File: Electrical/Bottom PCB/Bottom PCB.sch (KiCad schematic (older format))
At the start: 39 parts, among them J1 Steper1, J10 Servo4, J2 Steper2, J3 H Bridge, J4 4 x OP, J6 Servo1, J7 Servo2, J8 Servo3, J9 MainIO, SW1 FL, SW2 FR, U1 ULN2003A, U2 74HC595, U3 QRE1113, U4 TB6612FNG, U5 74HC595, U6 QRE1113, U7 QRE1113, U8 QRE1113

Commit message: small update
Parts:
- added C1, C11, C14, C2, C4, C7, C9: 100pF, Capacitor_SMD:C_1206_3216Metric_Pad1.42x1.75mm_HandSolder, symbol Device:C_Small
- added C10, C12, C3, C6, C8: 10uF, Capacitor_SMD:C_1206_3216Metric_Pad1.42x1.75mm_HandSolder, symbol Device:C_Small
- C13: renamed from C2; value 10pF -> 100pF; footprint Capacitor_SMD:C_1210_3225Metric_Pad1.42x2.65mm_HandSolder -> Capacitor_SMD:C_1206_3216Metric_Pad1.42x1.75mm_HandSolder
- C15: renamed from C3; value 10pF -> 100pF; footprint Capacitor_SMD:C_1210_3225Metric_Pad1.42x2.65mm_HandSolder -> Capacitor_SMD:C_1206_3216Metric_Pad1.42x1.75mm_HandSolder
- C16: renamed from C4; value 10pF -> 100pF
- C17: renamed from C5; value 10pF -> 100pF; footprint Capacitor_SMD:C_1210_3225Metric_Pad1.42x2.65mm_HandSolder -> Capacitor_SMD:C_1206_3216Metric_Pad1.42x1.75mm_HandSolder
- C5: renamed from C1; value 10pF -> 100pF; footprint Capacitor_SMD:C_1210_3225Metric_Pad1.42x2.65mm_HandSolder -> Capacitor_SMD:C_1206_3216Metric_Pad1.42x1.75mm_HandSolder
- J8: renamed from J9; footprint Connector_JST:JST_XH_B5B-XH-A_1x06_P2.50mm_Vertical -> Connector_PinHeader_2.54mm:PinHeader_1x06_P2.54mm_Vertical
- R1, R10, R11, R12, R2, R3, R4, R5, R6, R7, R8, R9: footprint Resistor_SMD:R_1210_3225Metric_Pad1.42x2.65mm_HandSolder -> Resistor_SMD:R_1206_3216Metric_Pad1.42x1.75mm_HandSolder
- renumbered J6 to J5, J7 to J6, J8 to J7, J10 to J9
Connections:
- wire segments 269 -> 294

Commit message: PCB
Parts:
- C16: footprint Capacitor_SMD:C_1210_3225Metric_Pad1.42x2.65mm_HandSolder -> Capacitor_SMD:C_1206_3216Metric_Pad1.42x1.75mm_HandSolder
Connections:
- wire segments 294 -> 295
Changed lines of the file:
@@
 Text GLabel 9350 3350 0    50   Input ~ 0
 Servo1
-Text GLabel 9350 3850 0    50   Input ~ 0
-Servo3
 Text GLabel 9350 3950 0    50   Input ~ 0
 Servo4
@@
 Wire Wire Line
 	6800 3800 6650 3800
-Text GLabel 9350 3650 0    50   Input ~ 0
-M1PWM
-Text GLabel 9350 3750 0    50   Input ~ 0
-M2PWM
 Text GLabel 5300 3300 0    50   Input ~ 0
 M2PWM
@@
 F 0 "C16" H 1492 5696 50  0000 L CNN
 F 1 "100pF" H 1492 5605 50  0000 L CNN
-F 2 "Capacitor_SMD:C_1210_3225Metric_Pad1.42x2.65mm_HandSolder" H 1400 5650 50  0001 C CNN
+F 2 "Capacitor_SMD:C_1206_3216Metric_Pad1.42x1.75mm_HandSolder" H 1400 5650 50  0001 C CNN
 F 3 "~" H 1400 5650 50  0001 C CNN
 	1    1400 5650
@@
 	11100 800  11250 800
 Connection ~ 11100 800
+Wire Wire Line
+	10500 3950 10650 3950
+Text GLabel 9350 3850 0    50   Input ~ 0
+Servo3
+Text GLabel 9350 3750 0    50   Input ~ 0
+M2PWM
+Text GLabel 9350 3650 0    50   Input ~ 0
+M1PWM
 $EndSCHEMATC

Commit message: Changed IR sensors to allow for passive measurments
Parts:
- removed J4: 4 x OP, Connector_PinHeader_2.54mm:PinHeader_1x04_P2.54mm_Vertical, symbol Connector_Generic:Conn_01x04
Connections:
- net labels added: IR

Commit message: Adding 9 DoF IMU
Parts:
- added C?: 10uF, Capacitor_SMD:C_1206_3216Metric_Pad1.42x1.75mm_HandSolder, symbol Device:C_Small
- added C?: 100pF, Capacitor_SMD:C_1206_3216Metric_Pad1.42x1.75mm_HandSolder, symbol Device:C_Small
- added U9: MPU-9250, Sensor_Motion:InvenSense_QFN-24_3x3mm_P0.4mm, symbol Sensor_Motion:MPU-9250
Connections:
- net labels added: +3.3V
- wire segments 295 -> 298
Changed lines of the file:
@@
 Text GLabel 550  6450 1    50   Input ~ 0
 IR
+$Comp
+L Sensor_Motion:MPU-9250 U9
+U 1 1 5ECB7562
+P 4500 6250
+F 0 "U9" H 4500 5261 50  0000 C CNN
+F 1 "MPU-9250" H 4500 5170 50  0000 C CNN
+F 2 "Sensor_Motion:InvenSense_QFN-24_3x3mm_P0.4mm" H 4500 5250 50  0001 C CNN
+F 3 "https://store.invensense.com/datasheets/invensense/MPU9250REV1.0.pdf" H 4500 6100 50  0001 C CNN
+	1    4500 6250
+	1    0    0    -1
+$EndComp
+$Comp
+L power:GND #PWR?
+U 1 1 5ECC16E7
+P 4500 7150
+F 0 "#PWR?" H 4500 6900 50  0001 C CNN
+F 1 "GND" H 4505 6977 50  0000 C CNN
+F 2 "" H 4500 7150 50  0001 C CNN
+F 3 "" H 4500 7150 50  0001 C CNN
+	1    4500 7150
+	1    0    0    -1
+$EndComp
+$Comp
+L power:GND #PWR?
+U 1 1 5ECC2609
+P 5350 7150
+F 0 "#PWR?" H 5350 6900 50  0001 C CNN
+F 1 "GND" H 5355 6977 50  0000 C CNN
+F 2 "" H 5350 7150 50  0001 C CNN
+F 3 "" H 5350 7150 50  0001 C CNN
+	1    5350 7150
+	1    0    0    -1
+$EndComp
+Wire Wire Line
+	5200 6650 5350 6650
+Wire Wire Line
+	5350 6650 5350 7150
+$Comp
+L power:+3.3V #PWR?
+U 1 1 5ECDED5D
+P 4600 5250
+F 0 "#PWR?" H 4600 5100 50  0001 C CNN
+F 1 "+3.3V" H 4615 5423 50  0000 C CNN
+F 2 "" H 4600 5250 50  0001 C CNN
+F 3 "" H 4600 5250 50  0001 C CNN
+	1    4600 5250
+	1    0    0    -1
+$EndComp
+Wire Wire Line
+	4600 5250 4600 5350
+$Comp
+L power:+3.3V #PWR?
+U 1 1 5ECFA0AC
+P 5450 5250
+F 0 "#PWR?" H 5450 5100 50  0001 C CNN
+F 1 "+3.3V" H 5465 5423 50  0000 C CNN
+F 2 "" H 5450 5250 50  0001 C CNN
+F 3 "" H 5450 5250 50  0001 C CNN
+	1    5450 5250
+	1    0    0    -1
+$EndComp
+$Comp
+L Device:C_Small C?
+U 1 1 5ECFABED
+P 5450 5350
+F 0 "C?" H 5542 5396 50  0000 L CNN
+F 1 "10uF" H 5542 5305 50  0000 L CNN
+F 2 "Capacitor_SMD:C_1206_3216Metric_Pad1.42x1.75mm_HandSolder" H 5450 5350 50  0001 C CNN
+F 3 "~" H 5450 5350 50  0001 C CNN
+	1    5450 5350
+	1    0    0    -1
+$EndComp
+$Comp
+L Device:C_Small C?
+U 1 1 5ECFB59E
+P 5800 5350
+F 0 "C?" H 5892 5396 50  0000 L CNN
+F 1 "100pF" H 5892 5305 50  0000 L CNN
+F 2 "Capacitor_SMD:C_1206_3216Metric_Pad1.42x1.75mm_HandSolder" H 5800 5350 50  0001 C CNN
+F 3 "~" H 5800 5350 50  0001 C CNN
+	1    5800 5350
+	1    0    0    -1
+$EndComp
+$Comp
+L power:+3.3V #PWR?
+U 1 1 5ECFBDFF
+P 5800 5250
+F 0 "#PWR?" H 5800 5100 50  0001 C CNN
+F 1 "+3.3V" H 5815 5423 50  0000 C CNN
+F 2 "" H 5800 5250 50  0001 C CNN
+F 3 "" H 5800 5250 50  0001 C CNN
+	1    5800 5250
+	1    0    0    -1
+$EndComp
+$Comp
+L power:GND #PWR?
+U 1 1 5ECFC360
+P 5450 5450
+F 0 "#PWR?" H 5450 5200 50  0001 C CNN
+F 1 "GND" H 5455 5277 50  0000 C CNN
+F 2 "" H 5450 5450 50  0001 C CNN
+F 3 "" H 5450 5450 50  0001 C CNN
+	1    5450 5450
+	1    0    0    -1
+$EndComp
+$Comp
+L power:GND #PWR?
+U 1 1 5ECFC83C
+P 5800 5450
+F 0 "#PWR?" H 5800 5200 50  0001 C CNN
+F 1 "GND" H 5805 5277 50  0000 C CNN
+F 2 "" H 5800 5450 50  0001 C CNN
+F 3 "" H 5800 5450 50  0001 C CNN
+	1    5800 5450
+	1    0    0    -1
+$EndComp
 $EndSCHEMATC

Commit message: Change MCU
swap arduino to ESP32-Wroom

https://www.mouser.co.uk/ProductDetail/Espressif/ESP32-WROVER/?qs=chTDxNqvsynCfB3ibKeA%252bA%3D%3D

Mouser No: 356-ESP32-WROVER
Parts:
- removed A1: Arduino_Nano_v3.x, Module:Arduino_Nano, symbol MCU_Module:Arduino_Nano_v3.x
- removed C11, C5: 100pF, Capacitor_SMD:C_1206_3216Metric_Pad1.42x1.75mm_HandSolder, symbol Device:C_Small
- removed C12: 10uF, Capacitor_SMD:C_1206_3216Metric_Pad1.42x1.75mm_HandSolder, symbol Device:C_Small
- removed U9: MPU-9250, Sensor_Motion:InvenSense_QFN-24_3x3mm_P0.4mm, symbol Sensor_Motion:MPU-9250
- added U10: MCP23017_SO, Package_SO:SOIC-28W_7.5x17.9mm_P1.27mm, symbol Interface_Expansion:MCP23017_SO
- added U9: ESP32-WROVER, esp32-wrover:ESP32-WROVER, symbol esp32-wrover:ESP32-WROVER
- R1: value 10k -> 22k
- gave numbers to parts that had none: 2
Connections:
- wire segments 298 -> 292
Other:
- moved on the sheet: C18, C19

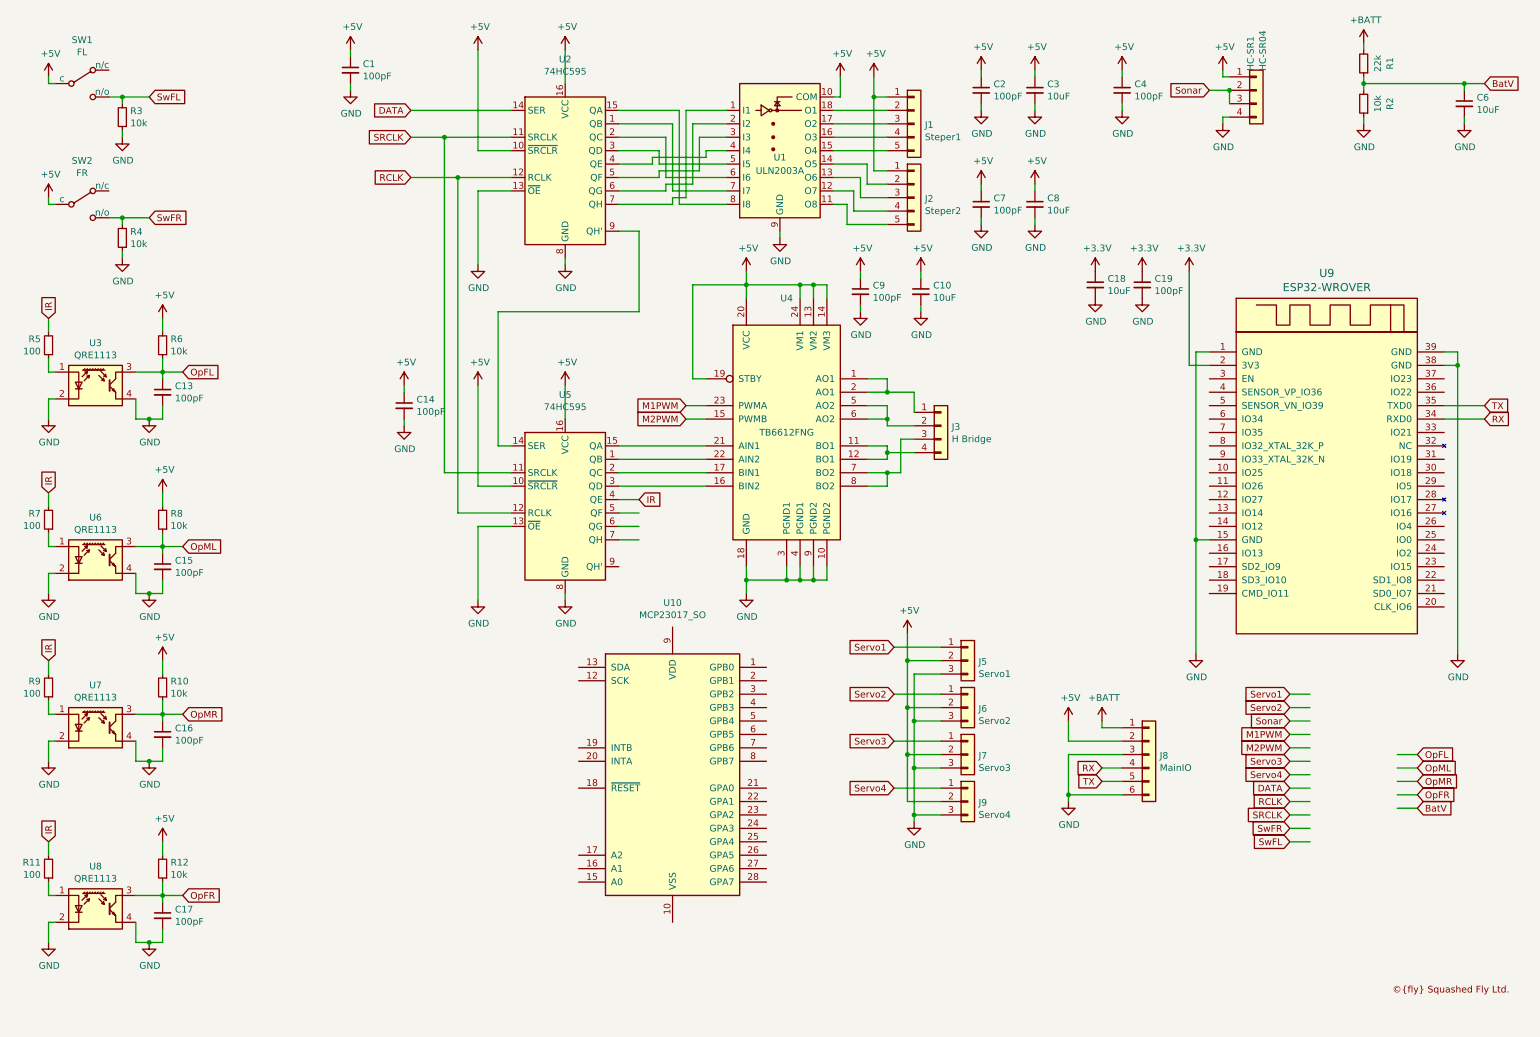
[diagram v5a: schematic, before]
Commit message: Add reset / reboot circuit for ESP32, modify readme to remove eagle constraint as eagle is no longer in use.
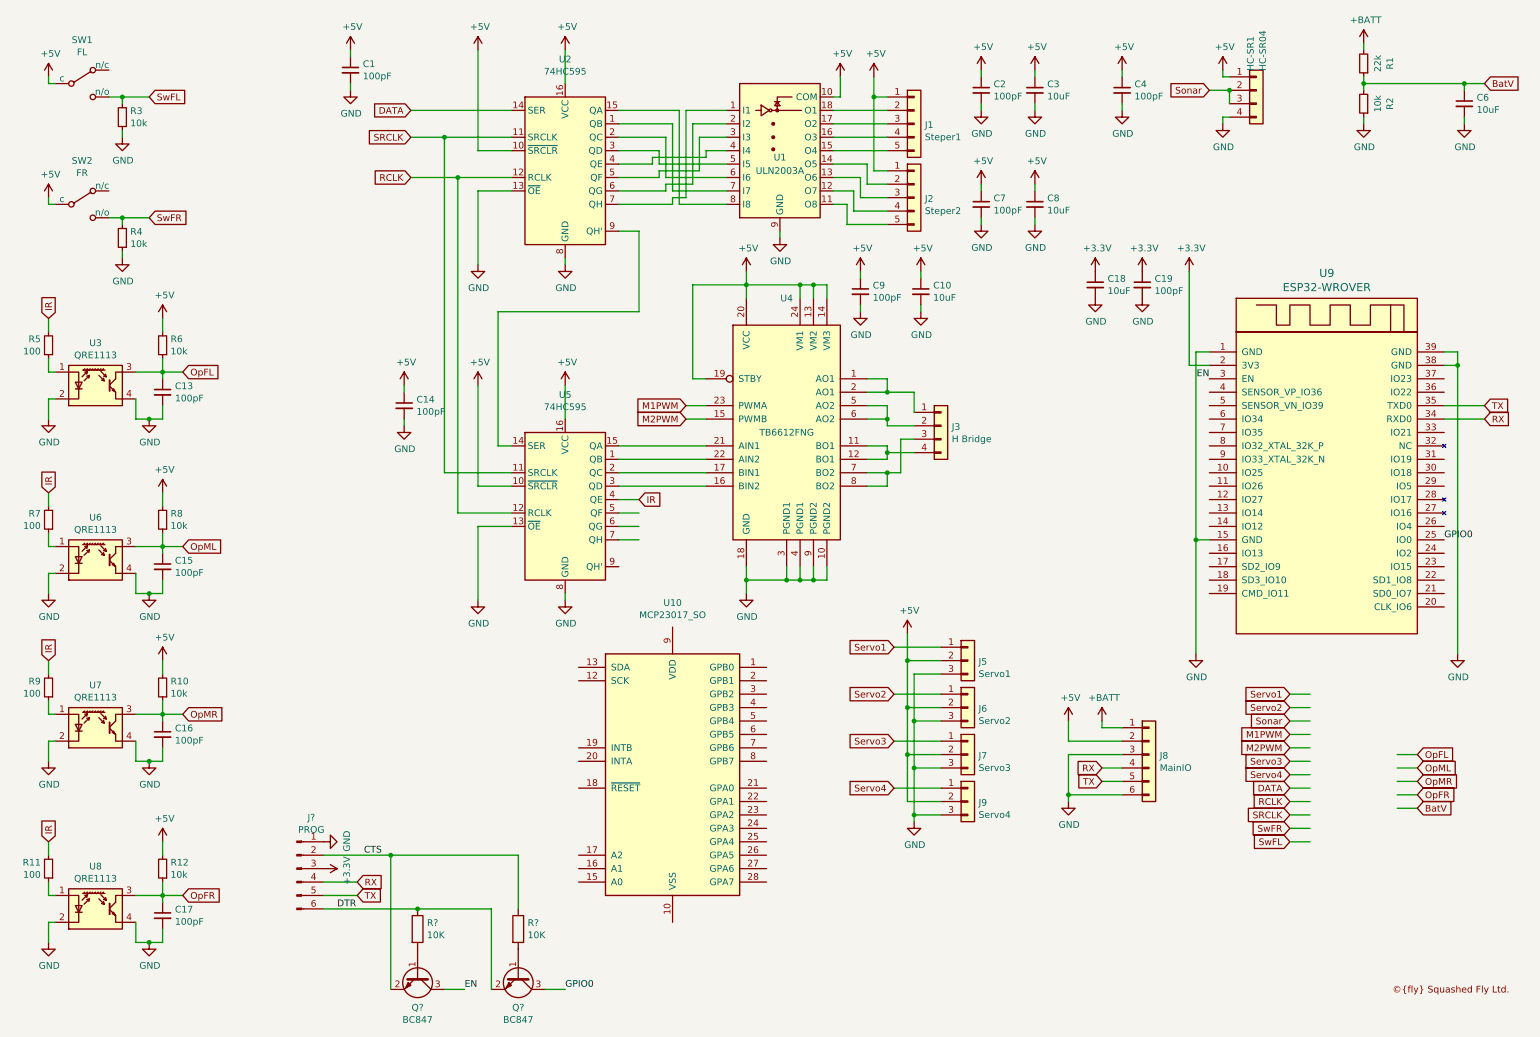
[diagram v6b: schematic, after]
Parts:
- added J?: PROG, Connector_PinHeader_2.54mm:PinHeader_1x06_P2.54mm_Vertical, symbol Connector:Conn_01x06_Male
- added Q? (x2): BC847, Package_TO_SOT_SMD:SOT-23, symbol Transistor_BJT:BC847
- added R? (x2): 10K, symbol Device:R
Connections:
- net labels added: CTS, DTR, EN, GPIO0
- wire segments 292 -> 303
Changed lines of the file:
@@
 EESchema Schematic File Version 4
-LIBS:Bottom PCB-cache
 EELAYER 30 0
 EELAYER END
@@
 	1    0    0    -1
 $EndComp
+$Comp
+L Connector:Conn_01x06_Male J?
+U 1 1 5EBE922C
+P 2400 6650
+F 0 "J?" H 2508 7031 50  0000 C CNN
+F 1 "PROG" H 2508 6940 50  0000 C CNN
+F 2 "Connector_PinHeader_2.54mm:PinHeader_1x06_P2.54mm_Vertical" H 2400 6650 50  0001 C CNN
+F 3 "~" H 2400 6650 50  0001 C CNN
+	1    2400 6650
+	1    0    0    -1
+$EndComp
+$Comp
+L power:GND #PWR?
+U 1 1 5EBEB3F9
+P 2600 6450
+F 0 "#PWR?" H 2600 6200 50  0001 C CNN
+F 1 "GND" H 2605 6277 50  0000 C CNN
+F 2 "" H 2600 6450 50  0001 C CNN
+F 3 "" H 2600 6450 50  0001 C CNN
+	1    2600 6450
+	0    -1   -1   0
+$EndComp
+Wire Wire Line
+	2600 6750 2850 6750
+Wire Wire Line
+	2600 6850 2850 6850
+$Comp
+L power:+3.3V #PWR?
+U 1 1 5EC6FB03
+P 2600 6650
+F 0 "#PWR?" H 2600 6500 50  0001 C CNN
+F 1 "+3.3V" H 2615 6823 50  0000 C CNN
+F 2 "" H 2600 6650 50  0001 C CNN
+F 3 "" H 2600 6650 50  0001 C CNN
+	1    2600 6650
+	0    1    1    0
+$EndComp
+Text GLabel 2850 6850 2    49   Input ~ 0
+TX
+Text GLabel 2850 6750 2    49   Input ~ 0
+RX
+$Comp
+L Transistor_BJT:BC847 Q?
+U 1 1 5EC84C0A
+P 4050 7450
+F 0 "Q?" V 4285 7450 50  0000 C CNN
+F 1 "BC847" V 4376 7450 50  0000 C CNN
+F 2 "Package_TO_SOT_SMD:SOT-23" H 4250 7375 50  0001 L CIN
+F 3 "http://www.infineon.com/dgdl/Infineon-BC847SERIES_BC848SERIES_BC849SERIES_BC850SERIES-DS-v01_01-en.pdf?fileId=db3a304314dca389011541d4630a1657" H 4050 7450 50  0001 L CNN
+	1    4050 7450
+	0    1    1    0
+$EndComp
+$Comp
+L Transistor_BJT:BC847 Q?
+U 1 1 5EC854CB
+P 3300 7450
+F 0 "Q?" V 3535 7450 50  0000 C CNN
+F 1 "BC847" V 3626 7450 50  0000 C CNN
+F 2 "Package_TO_SOT_SMD:SOT-23" H 3500 7375 50  0001 L CIN
+F 3 "http://www.infineon.com/dgdl/Infineon-BC847SERIES_BC848SERIES_BC849SERIES_BC850SERIES-DS-v01_01-en.pdf?fileId=db3a304314dca389011541d4630a1657" H 3300 7450 50  0001 L CNN
+	1    3300 7450
+	0    1    1    0
+$EndComp
+Wire Wire Line
+	4050 6550 4050 6950
+Wire Wire Line
+	2600 6550 3100 6550
+Wire Wire Line
+	3100 7550 3100 6550
+Connection ~ 3100 6550
+Wire Wire Line
+	3100 6550 4050 6550
+Wire Wire Line
+	3850 6950 3850 7550
+Wire Wire Line
+	2600 6950 3300 6950
+Connection ~ 3300 6950
+Wire Wire Line
+	3300 6950 3850 6950
+Wire Wire Line
+	3500 7550 3650 7550
+Wire Wire Line
+	4250 7550 4400 7550
+$Comp
+L Device:R R?
+U 1 1 5ED6B6F5
+P 3300 7100
+F 0 "R?" H 3370 7146 50  0000 L CNN
+F 1 "10K" H 3370 7055 50  0000 L CNN
+F 2 "" V 3230 7100 50  0001 C CNN
+F 3 "~" H 3300 7100 50  0001 C CNN
+	1    3300 7100
+	1    0    0    -1
+$EndComp
+$Comp
+L Device:R R?
+U 1 1 5ED6BE05
+P 4050 7100
+F 0 "R?" H 4120 7146 50  0000 L CNN
+F 1 "10K" H 4120 7055 50  0000 L CNN
+F 2 "" V 3980 7100 50  0001 C CNN
+F 3 "~" H 4050 7100 50  0001 C CNN
+	1    4050 7100
+	1    0    0    -1
+$EndComp
+Text Label 2700 6950 0    50   ~ 0
+DTR
+Text Label 2900 6550 0    50   ~ 0
+CTS
+Text Label 3650 7550 0    50   ~ 0
+EN
+Text Label 4400 7550 0    50   ~ 0
+GPIO0
+Text Label 9200 3000 2    50   ~ 0
+EN
+Text Label 10950 4200 0    50   ~ 0
+GPIO0
 $EndSCHEMATC

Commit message: Moved components to sub sheets
Continued on from Bob's work, in so much that I moved some items to additional sheets, increesed the size of the main header to include a half battery tap, and the addition of jumpers so that the device can be re-programmed without disasembly (however will need a soldering iron). may change this to a three way jumper at a later date,
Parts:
- removed C18, C3, C6: 10uF, Capacitor_SMD:C_1206_3216Metric_Pad1.42x1.75mm_HandSolder, symbol Device:C_Small
- removed C19, C2: 100pF, Capacitor_SMD:C_1206_3216Metric_Pad1.42x1.75mm_HandSolder, symbol Device:C_Small
- removed J8: MainIO, Connector_PinHeader_2.54mm:PinHeader_1x06_P2.54mm_Vertical, symbol Connector_Generic:Conn_01x06
- removed J?: PROG, Connector_PinHeader_2.54mm:PinHeader_1x06_P2.54mm_Vertical, symbol Connector:Conn_01x06_Male
- removed Q? (x2): BC847, Package_TO_SOT_SMD:SOT-23, symbol Transistor_BJT:BC847
- removed R1: 22k, Resistor_SMD:R_1206_3216Metric_Pad1.42x1.75mm_HandSolder, symbol Device:R_Small
- removed R2: 10k, Resistor_SMD:R_1206_3216Metric_Pad1.42x1.75mm_HandSolder, symbol Device:R_Small
- removed R? (x2): 10K, symbol Device:R
- removed U9: ESP32-WROVER, esp32-wrover:ESP32-WROVER, symbol esp32-wrover:ESP32-WROVER
- renumbered C1 to C101, C4 to C102, C7 to C103, C8 to C104, C9 to C105, C10 to C106, C13 to C107, C14 to C108, C15 to C109, C16 to C110, C17 to C111, HC-SR1 to HC-SR101, J1 to J101, J2 to J102, J3 to J103, J5 to J104, J6 to J105, J7 to J106, J9 to J107, Logo1 to Logo101, R3 to R101, R4 to R102, R5 to R103, R6 to R104, R7 to R105, R8 to R106, R9 to R107, R10 to R108, R11 to R109, R12 to R110, SW1 to SW101, SW2 to SW102, U1 to U101, U2 to U102, U3 to U103, U4 to U104, U5 to U105, U6 to U106, U7 to U107, U10 to U108, U8 to U109
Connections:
- net labels removed: +3.3V, +BATT, BatV, CTS, DTR, EN, GPIO0, RX, TX
- wire segments 303 -> 241
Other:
- moved on the sheet: U108
